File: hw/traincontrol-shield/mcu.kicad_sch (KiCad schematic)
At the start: 7 parts, among them J1 ESP32-S3 Header L, J2 ESP32-S3 Header R

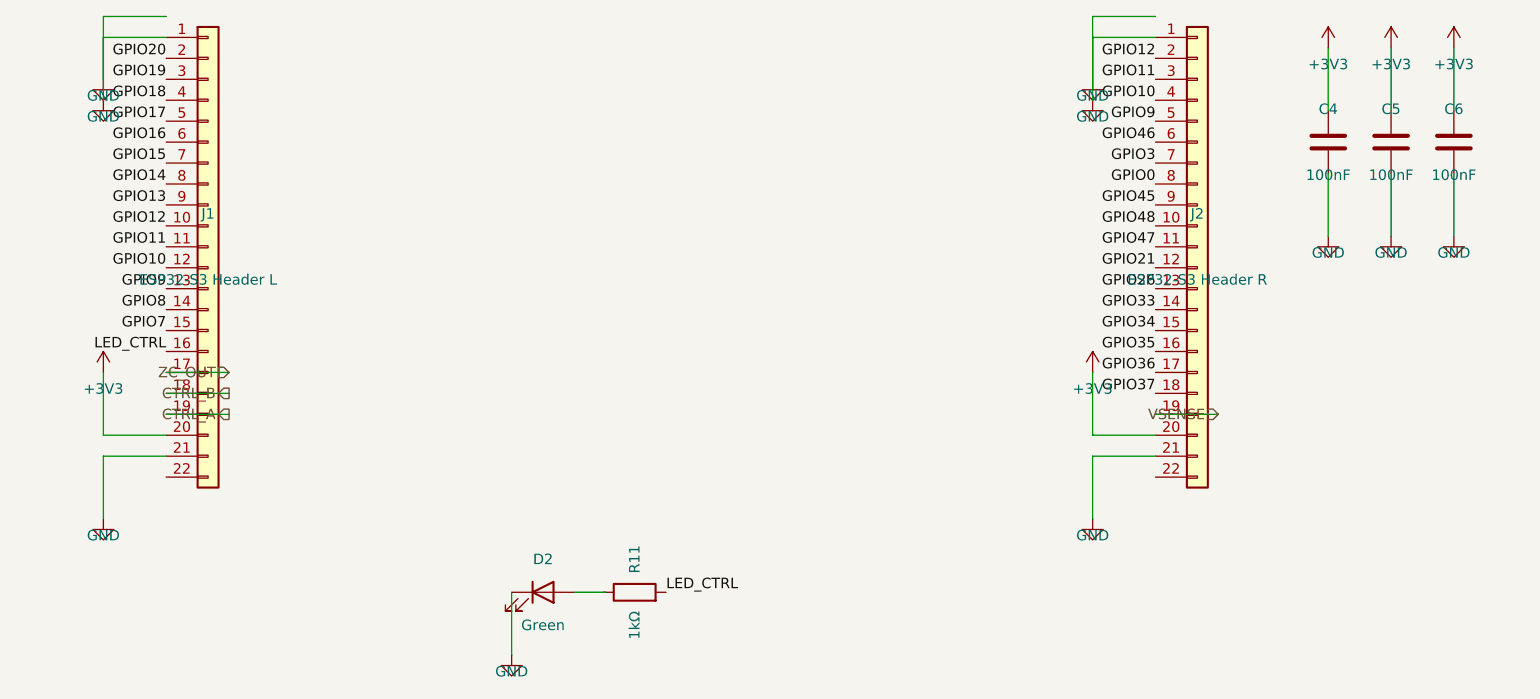
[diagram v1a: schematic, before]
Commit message: Fix hierarchical label placement and orientation in sub-sheets
Root cause: hlabel() placed the label at lx (stub tip) instead of x
(circuit connection point), mirroring the Issue-2 glabel bug fixed in
commit 2270223.

Fix applied to hlabel():
  (at {lx} ...) → (at {x} ...)  — label now sits at the circuit endpoint

Angle convention (matches label body direction):
  angle=180 → body extends LEFT  — left-side input/bidirectional labels
  angle=0   → body extends RIGHT — right-side output/bidirectional labels

Sheets affected: zero-crossing, xor-interlock, opto-triac-drive,
rail-voltage-sense; triacs-snubbers and mcu already had correct angles.

Co-Authored-By: Claude Sonnet 4.6 <noreply@anthropic.com>
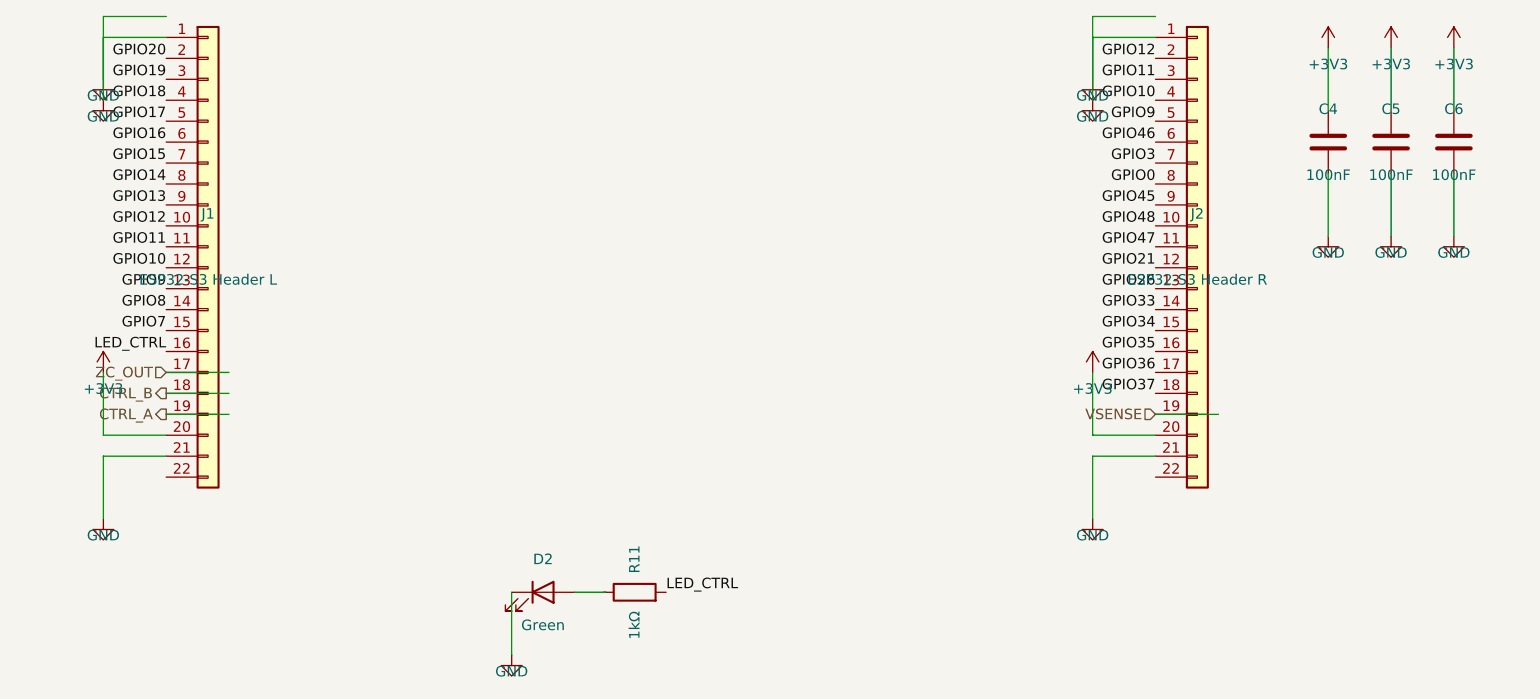
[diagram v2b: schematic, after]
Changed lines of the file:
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@@
 	(hierarchical_label "CTRL_A"
 		(shape output)
-		(at 82.55000000000001 140.97 180)
-		(fields_autoplaced yes)
-		(effects (font (size 1.27 1.27)) (justify right bottom))
-		(property "Intersheetrefs" "${INTERSHEET_REFS}"
-			(at 82.55000000000001 140.97 0)
+		(at 74.93 140.97 180)
+		(fields_autoplaced yes)
+		(effects (font (size 1.27 1.27)) (justify right bottom))
+		(property "Intersheetrefs" "${INTERSHEET_REFS}"
+			(at 74.93 140.97 0)
 			(effects (font (size 1.27 1.27)) (hide yes))
 		)
@@
 	(hierarchical_label "CTRL_B"
 		(shape output)
-		(at 82.55000000000001 138.43 180)
-		(fields_autoplaced yes)
-		(effects (font (size 1.27 1.27)) (justify right bottom))
-		(property "Intersheetrefs" "${INTERSHEET_REFS}"
-			(at 82.55000000000001 138.43 0)
+		(at 74.93 138.43 180)
+		(fields_autoplaced yes)
+		(effects (font (size 1.27 1.27)) (justify right bottom))
+		(property "Intersheetrefs" "${INTERSHEET_REFS}"
+			(at 74.93 138.43 0)
 			(effects (font (size 1.27 1.27)) (hide yes))
 		)
@@
 	(hierarchical_label "ZC_OUT"
 		(shape input)
-		(at 82.55000000000001 135.89 180)
-		(fields_autoplaced yes)
-		(effects (font (size 1.27 1.27)) (justify right bottom))
-		(property "Intersheetrefs" "${INTERSHEET_REFS}"
-			(at 82.55000000000001 135.89 0)
+		(at 74.93 135.89 180)
+		(fields_autoplaced yes)
+		(effects (font (size 1.27 1.27)) (justify right bottom))
+		(property "Intersheetrefs" "${INTERSHEET_REFS}"
+			(at 74.93 135.89 0)
 			(effects (font (size 1.27 1.27)) (hide yes))
 		)
@@
 	(hierarchical_label "VSENSE"
 		(shape input)
-		(at 202.56 140.97 180)
-		(fields_autoplaced yes)
-		(effects (font (size 1.27 1.27)) (justify right bottom))
-		(property "Intersheetrefs" "${INTERSHEET_REFS}"
-			(at 202.56 140.97 0)
-			(effects (font (size 1.27 1.27)) (hide yes))
-		)
+		(at 194.94 140.97 180)
+		(fields_autoplaced yes)
+		(effects (font (size 1.27 1.27)) (justify right bottom))
+		(property "Intersheetrefs" "${INTERSHEET_REFS}"
+			(at 194.94 140.97 0)
+			(effects (font (size 1.27 1.27)) (hide yes))
+		)

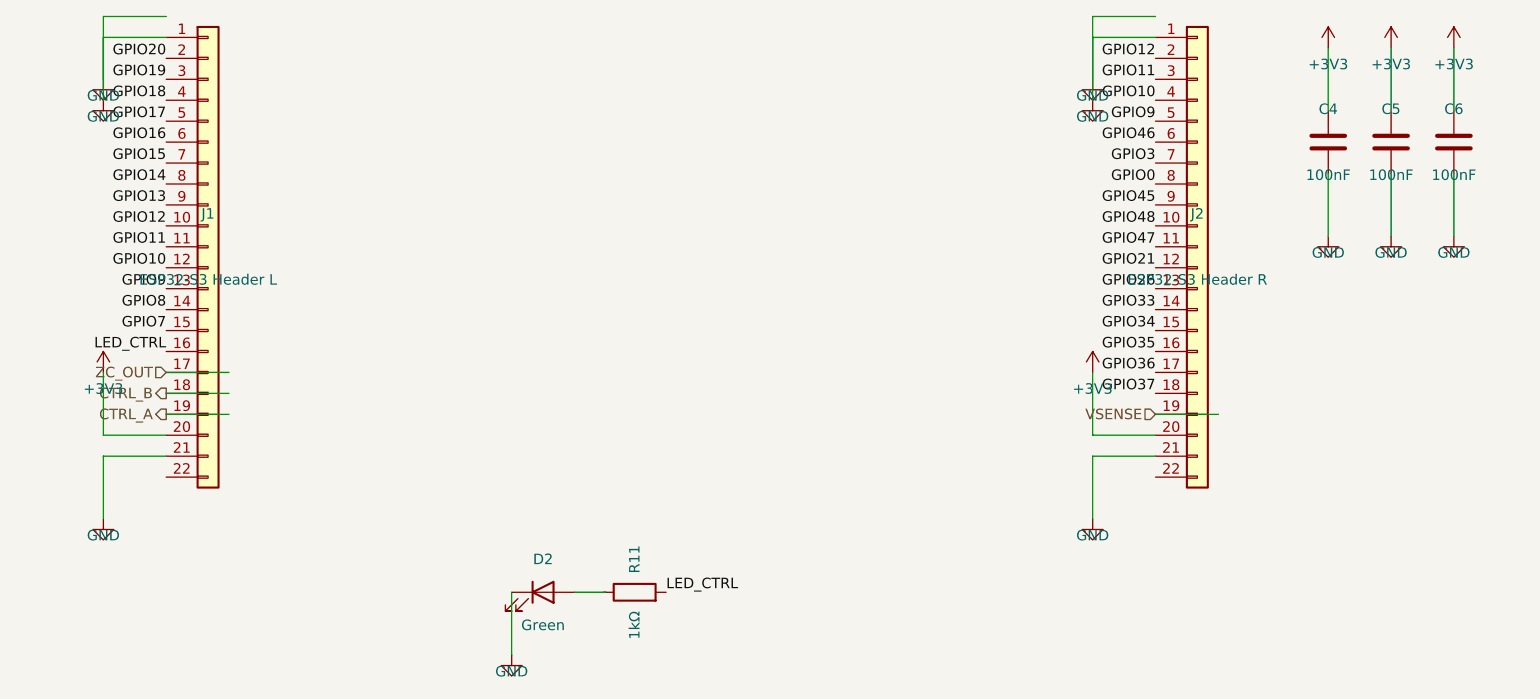
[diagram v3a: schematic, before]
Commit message: Fix hlabel stub direction: stubs now extend away from IC, not into it
Root cause: hlabel() used dx = +STUB for angle=180 and -STUB for angle=0,
which caused every stub wire to run INTO the IC body instead of outward.
This made wires appear to connect at the inner (wrong) end of all pins.

Fix: negate dx so stubs always extend outward from the pin tip:
  angle=180 (left-side input):  dx = -STUB → stub extends LEFT  ✓
  angle=0   (right-side output): dx = +STUB → stub extends RIGHT ✓

Also revert the x-position workarounds that compensated for the wrong
stub direction (zero-crossing AC_IN, opto-triac PHASE/GATE, power-supply
AC_IN/RTN): these are now back at the actual component pin positions.

All 8 sheets validate with kicad-cli.

Co-Authored-By: Claude Sonnet 4.6 <noreply@anthropic.com>
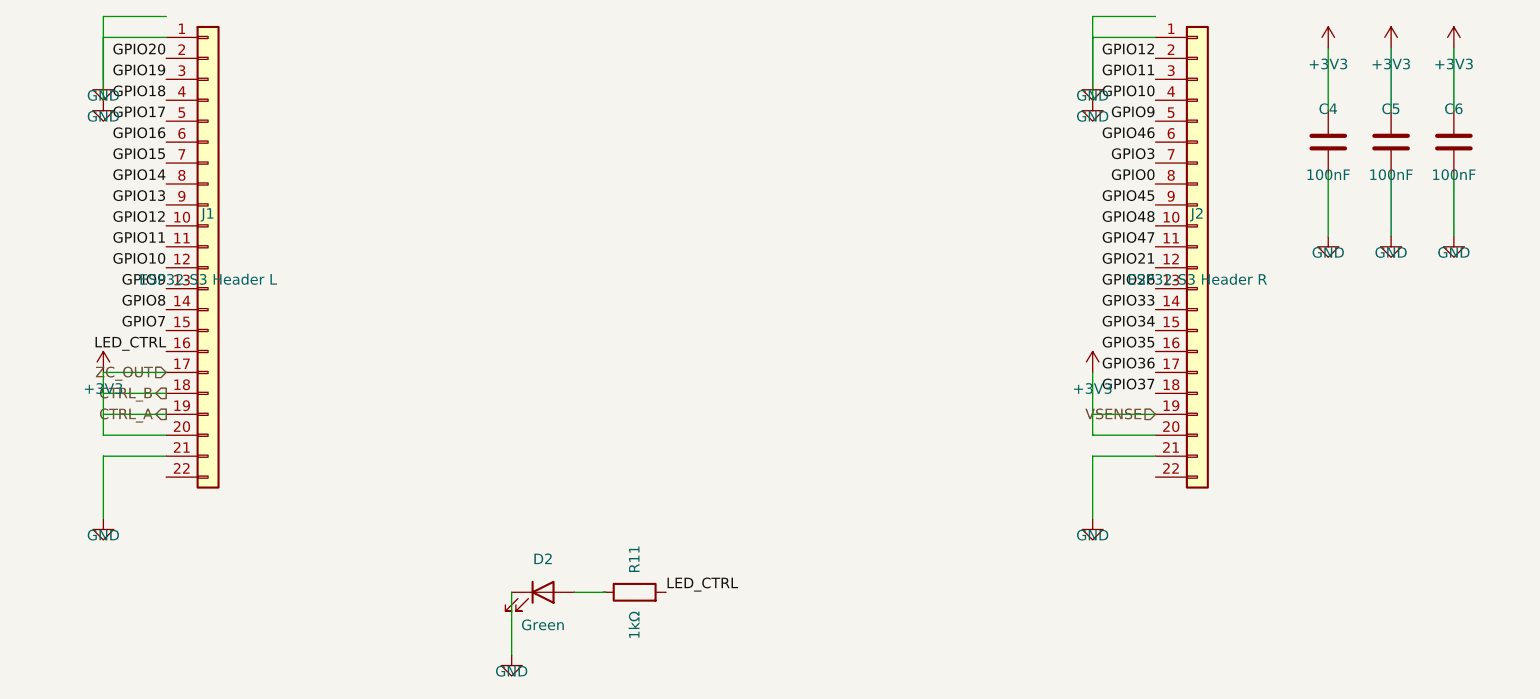
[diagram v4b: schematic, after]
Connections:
- net ZC_OUT is gone; now on net +3V3: J1.17 (Pin_17)
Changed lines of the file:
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@@
 	)
 	(wire
-		(pts (xy 74.93 140.97) (xy 82.55000000000001 140.97))
+		(pts (xy 67.31 140.97) (xy 74.93 140.97))
 		(stroke (width 0) (type solid))
 	)
@@
 	)
 	(wire
-		(pts (xy 74.93 138.43) (xy 82.55000000000001 138.43))
+		(pts (xy 67.31 138.43) (xy 74.93 138.43))
 		(stroke (width 0) (type solid))
 	)
@@
 	)
 	(wire
-		(pts (xy 74.93 135.89) (xy 82.55000000000001 135.89))
+		(pts (xy 67.31 135.89) (xy 74.93 135.89))
 		(stroke (width 0) (type solid))
 	)
@@
 	)
 	(wire
-		(pts (xy 194.94 140.97) (xy 202.56 140.97))
-		(stroke (width 0) (type solid))
-	)
+		(pts (xy 187.32 140.97) (xy 194.94 140.97))
+		(stroke (width 0) (type solid))
+	)

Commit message: Fix hlabel placement: label sits at stub outer end (lx), not pin tip (x)
The hierarchical label connection point must be at lx (the outer end of
the stub wire), not at x (the IC pin tip). With the label at x, it was
overlapping the pin itself instead of sitting at the end of the routing
stub where it belongs.

  angle=180 (left-side): lx = x - STUB  → label to the left of pin ✓
  angle=0   (right-side): lx = x + STUB  → label to the right of pin ✓

Wire still runs x↔lx, connecting the IC pin to the label connection.
Updated gen_all_sheets.py and gen_power_supply.py.

Co-Authored-By: Claude Sonnet 4.6 <noreply@anthropic.com>
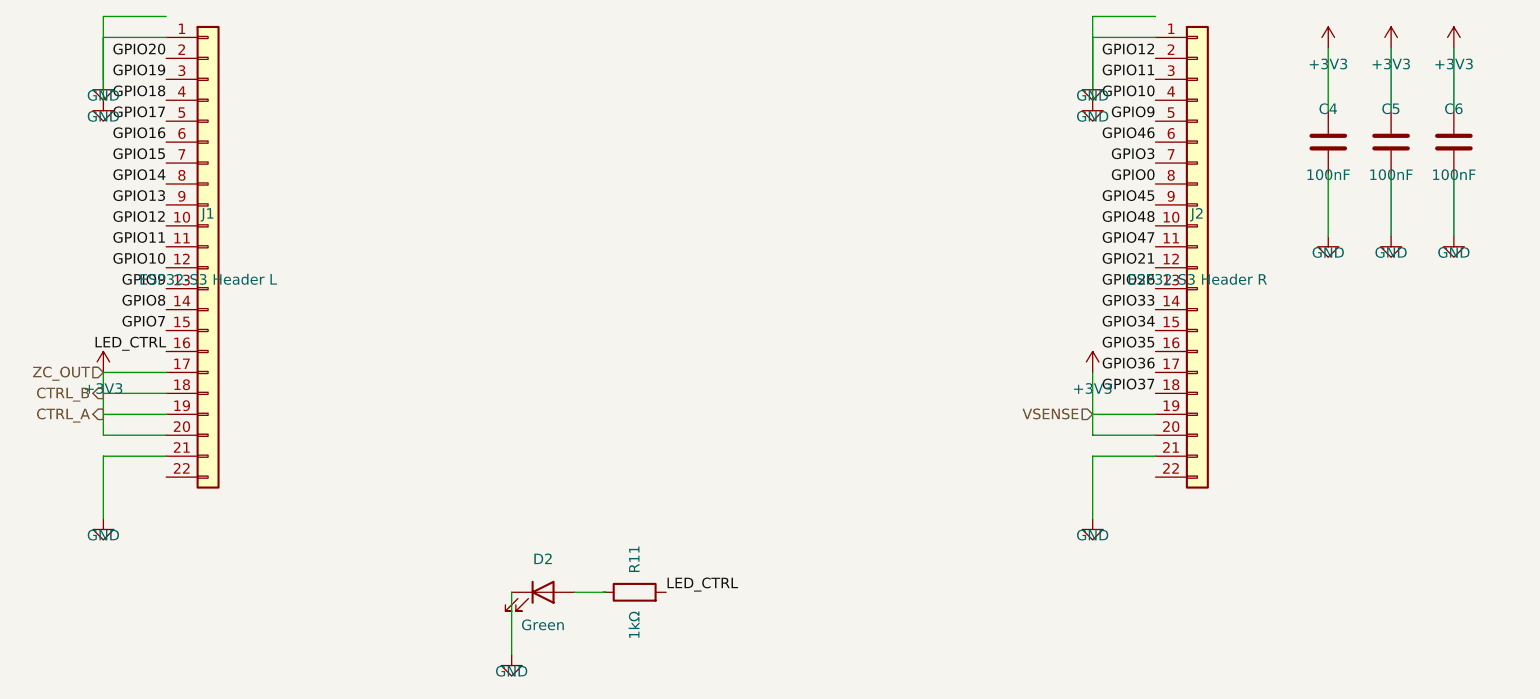
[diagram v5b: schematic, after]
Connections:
- net CTRL_A is gone; now on net +3V3: J1.19 (Pin_19)
- net CTRL_B is gone; now on net +3V3: J1.18 (Pin_18)
- net VSENSE is gone; now on net +3V3: J2.19 (Pin_19)
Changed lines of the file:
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@@
 	(hierarchical_label "CTRL_A"
 		(shape output)
-		(at 74.93 140.97 180)
-		(fields_autoplaced yes)
-		(effects (font (size 1.27 1.27)) (justify right bottom))
-		(property "Intersheetrefs" "${INTERSHEET_REFS}"
-			(at 74.93 140.97 0)
+		(at 67.31 140.97 180)
+		(fields_autoplaced yes)
+		(effects (font (size 1.27 1.27)) (justify right bottom))
+		(property "Intersheetrefs" "${INTERSHEET_REFS}"
+			(at 67.31 140.97 0)
 			(effects (font (size 1.27 1.27)) (hide yes))
 		)
@@
 	(hierarchical_label "CTRL_B"
 		(shape output)
-		(at 74.93 138.43 180)
-		(fields_autoplaced yes)
-		(effects (font (size 1.27 1.27)) (justify right bottom))
-		(property "Intersheetrefs" "${INTERSHEET_REFS}"
-			(at 74.93 138.43 0)
+		(at 67.31 138.43 180)
+		(fields_autoplaced yes)
+		(effects (font (size 1.27 1.27)) (justify right bottom))
+		(property "Intersheetrefs" "${INTERSHEET_REFS}"
+			(at 67.31 138.43 0)
 			(effects (font (size 1.27 1.27)) (hide yes))
 		)
@@
 	(hierarchical_label "ZC_OUT"
 		(shape input)
-		(at 74.93 135.89 180)
-		(fields_autoplaced yes)
-		(effects (font (size 1.27 1.27)) (justify right bottom))
-		(property "Intersheetrefs" "${INTERSHEET_REFS}"
-			(at 74.93 135.89 0)
+		(at 67.31 135.89 180)
+		(fields_autoplaced yes)
+		(effects (font (size 1.27 1.27)) (justify right bottom))
+		(property "Intersheetrefs" "${INTERSHEET_REFS}"
+			(at 67.31 135.89 0)
 			(effects (font (size 1.27 1.27)) (hide yes))
 		)
@@
 	(hierarchical_label "VSENSE"
 		(shape input)
-		(at 194.94 140.97 180)
-		(fields_autoplaced yes)
-		(effects (font (size 1.27 1.27)) (justify right bottom))
-		(property "Intersheetrefs" "${INTERSHEET_REFS}"
-			(at 194.94 140.97 0)
-			(effects (font (size 1.27 1.27)) (hide yes))
-		)
+		(at 187.32 140.97 180)
+		(fields_autoplaced yes)
+		(effects (font (size 1.27 1.27)) (justify right bottom))
+		(property "Intersheetrefs" "${INTERSHEET_REFS}"
+			(at 187.32 140.97 0)
+			(effects (font (size 1.27 1.27)) (hide yes))
+		)

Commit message: Add wire stub to net_label, matching hlabel placement convention
net_label() now generates a short wire stub (length STUB) between the
component pin tip (x) and the label connection point (lx), placing the
label at the outer end of the stub — identical to how hlabel works:

  angle=180 (left-side):  lx = x - STUB, label left of pin  ✓
  angle=0   (right-side): lx = x + STUB, label right of pin ✓

Also fix XOR_OUT net labels at U4A/B left-side input pins (angle=0→180)
so their stubs extend leftward away from the IC body.

Updated gen_all_sheets.py and gen_power_supply.py.

Co-Authored-By: Claude Sonnet 4.6 <noreply@anthropic.com>
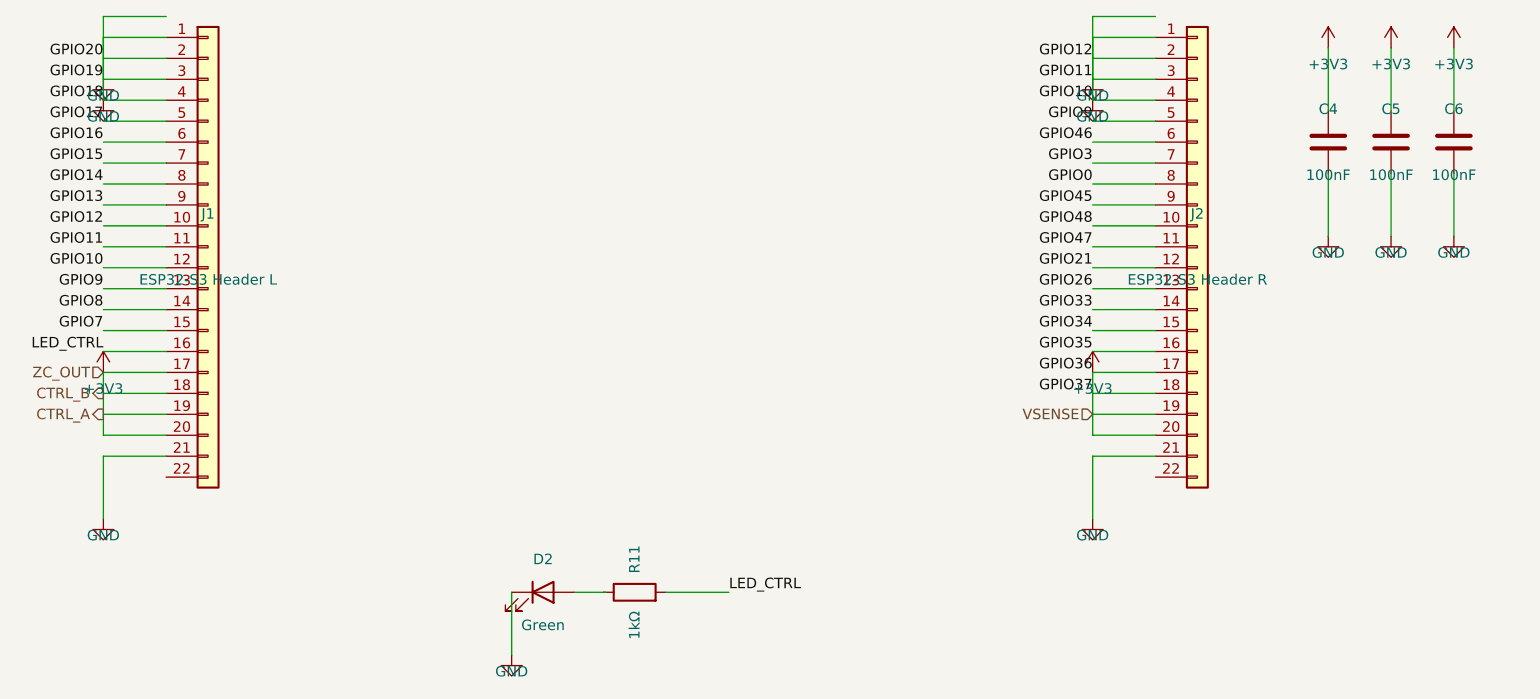
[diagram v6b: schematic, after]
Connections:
- net GPIO10 is gone; now on net GND: J1.12 (Pin_12), J2.4 (Pin_4)
- net GPIO11 is gone; now on net GND: J1.11 (Pin_11), J2.3 (Pin_3)
- net GPIO12 is gone; now on net GND: J1.10 (Pin_10), J2.2 (Pin_2)
- net GPIO18 is gone; now on net GND: J1.4 (Pin_4)
- net GPIO19 is gone; now on net GND: J1.3 (Pin_3)
- net GPIO20 is gone; now on net GND: J1.2 (Pin_2)
- net GPIO36 is gone; now on net +3V3: J2.17 (Pin_17)
- net GPIO37 is gone; now on net +3V3: J2.18 (Pin_18)
